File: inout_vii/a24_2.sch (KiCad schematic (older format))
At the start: 21 parts, among them U24010 74HC27, U24011 74LVC07, U24012 74HC02, U24013 74HC27, U24014 74HC02, U24015 74HC4002, U24016 74HC27, U24017 74LVC07, U24018 74HC02, U24019 74HC27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

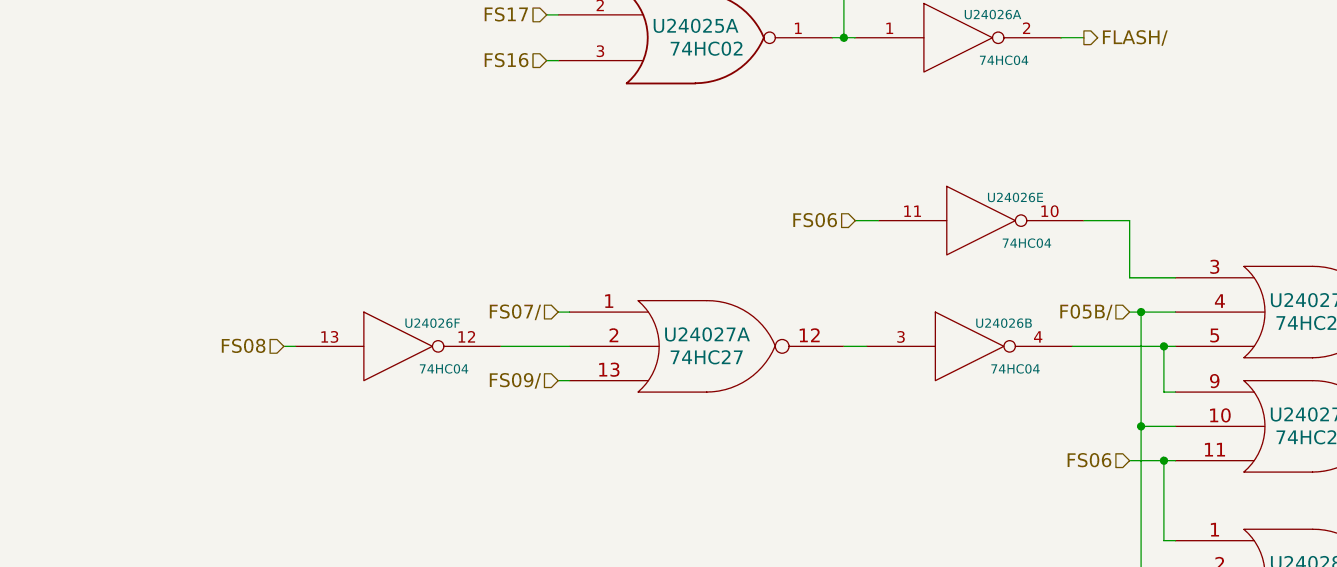
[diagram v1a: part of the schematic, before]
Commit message: Added some missing net names.
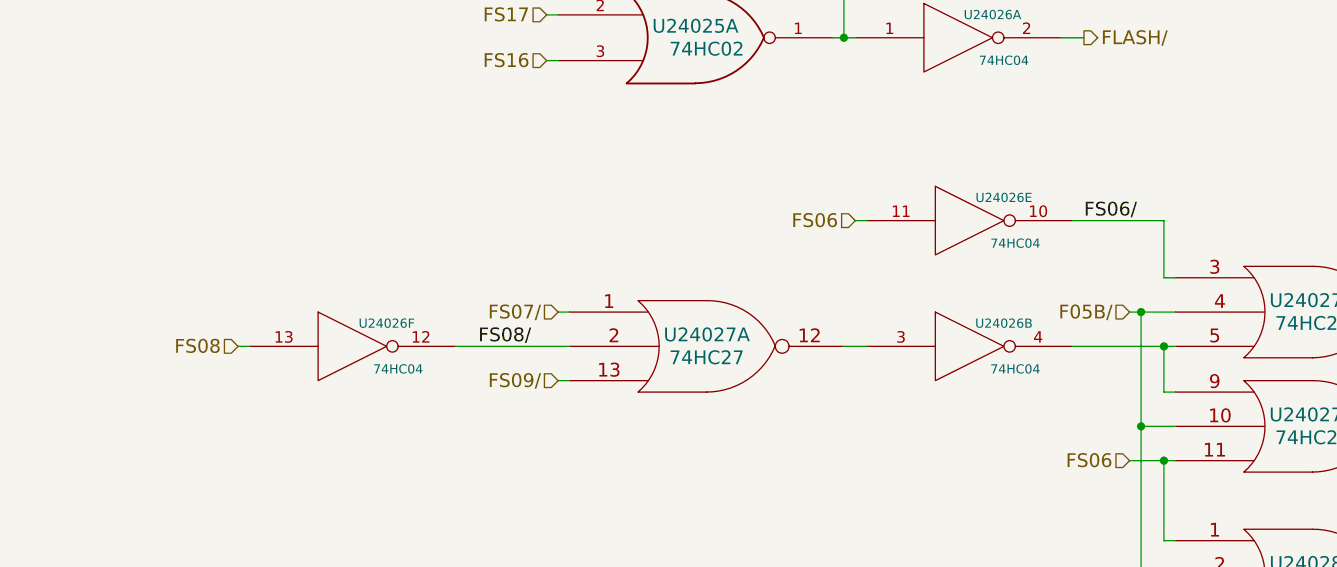
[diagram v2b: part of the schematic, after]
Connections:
- net FS08/: now reaches U24026.12, U24027.2
- net FS06/: now reaches U24026.10, U24027.3
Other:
- moved on the sheet: U24026E, U24026F
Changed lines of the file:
@@
 Wire Wire Line
 	9300 4300 9350 4300
-Text HLabel 8100 4450 0    60   Input ~ 0
+Text HLabel 7900 4450 0    60   Input ~ 0
 FS08
 Wire Wire Line
-	9050 4450 9350 4450
+	8850 4450 9350 4450
 Text HLabel 9300 4600 0    60   Input ~ 0
 FS09/
@@
 FS06
 Wire Wire Line
-	11800 4150 12000 4150
+	11950 4150 12000 4150
 Text HLabel 11800 4300 0    60   Input ~ 0
 F05B/
@@
 L 74HC04 U24026
 U 5 1 57212A45
-P 11150 3900
-F 0 "U24026" H 11300 4000 40  0000 C CNN
-F 1 "74HC04" H 11350 3800 40  0000 C CNN
-F 2 "" H 11150 3900 60  0000 C CNN
-F 3 "" H 11150 3900 60  0000 C CNN
-	5    11150 3900
-	1    0    0    -1
-$EndComp
-Wire Wire Line
-	10600 3900 10700 3900
-Wire Wire Line
-	11800 4150 11800 3900
-Wire Wire Line
-	11800 3900 11600 3900
+P 11100 3900
+F 0 "U24026" H 11250 4000 40  0000 C CNN
+F 1 "74HC04" H 11300 3800 40  0000 C CNN
+F 2 "" H 11100 3900 60  0000 C CNN
+F 3 "" H 11100 3900 60  0000 C CNN
+	5    11100 3900
+	1    0    0    -1
+$EndComp
+Wire Wire Line
+	10600 3900 10650 3900
+Wire Wire Line
+	11950 4150 11950 3900
+Wire Wire Line
+	11950 3900 11550 3900
 $Comp
 L 74HC04 U24026
 U 6 1 5721963E
-P 8600 4450
-F 0 "U24026" H 8750 4550 40  0000 C CNN
-F 1 "74HC04" H 8800 4350 40  0000 C CNN
-F 2 "" H 8600 4450 60  0000 C CNN
-F 3 "" H 8600 4450 60  0000 C CNN
-	6    8600 4450
-	1    0    0    -1
-$EndComp
-Wire Wire Line
-	8100 4450 8150 4450
+P 8400 4450
+F 0 "U24026" H 8550 4550 40  0000 C CNN
+F 1 "74HC04" H 8600 4350 40  0000 C CNN
+F 2 "" H 8400 4450 60  0000 C CNN
+F 3 "" H 8400 4450 60  0000 C CNN
+	6    8400 4450
+	1    0    0    -1
+$EndComp
+Wire Wire Line
+	7900 4450 7950 4450
+Text Label 8950 4450 0    60   ~ 0
+FS08/
+Text Label 11600 3900 0    60   ~ 0
+FS06/
 $EndSCHEMATC

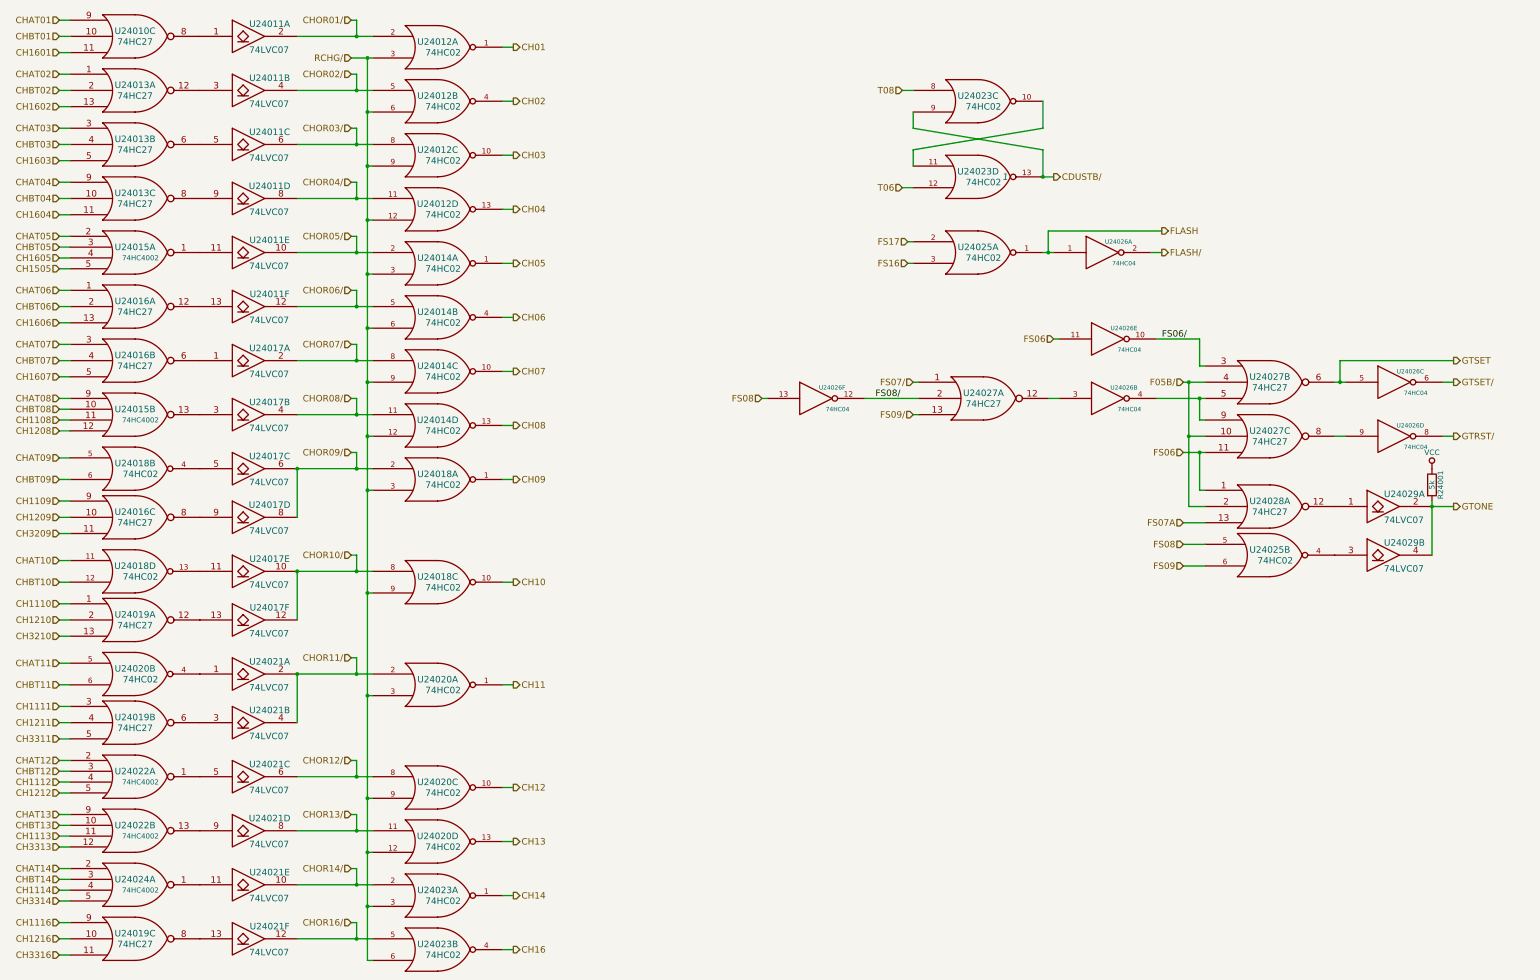
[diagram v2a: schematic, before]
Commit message: Fixed not->1-input nor in the rest of the modules.
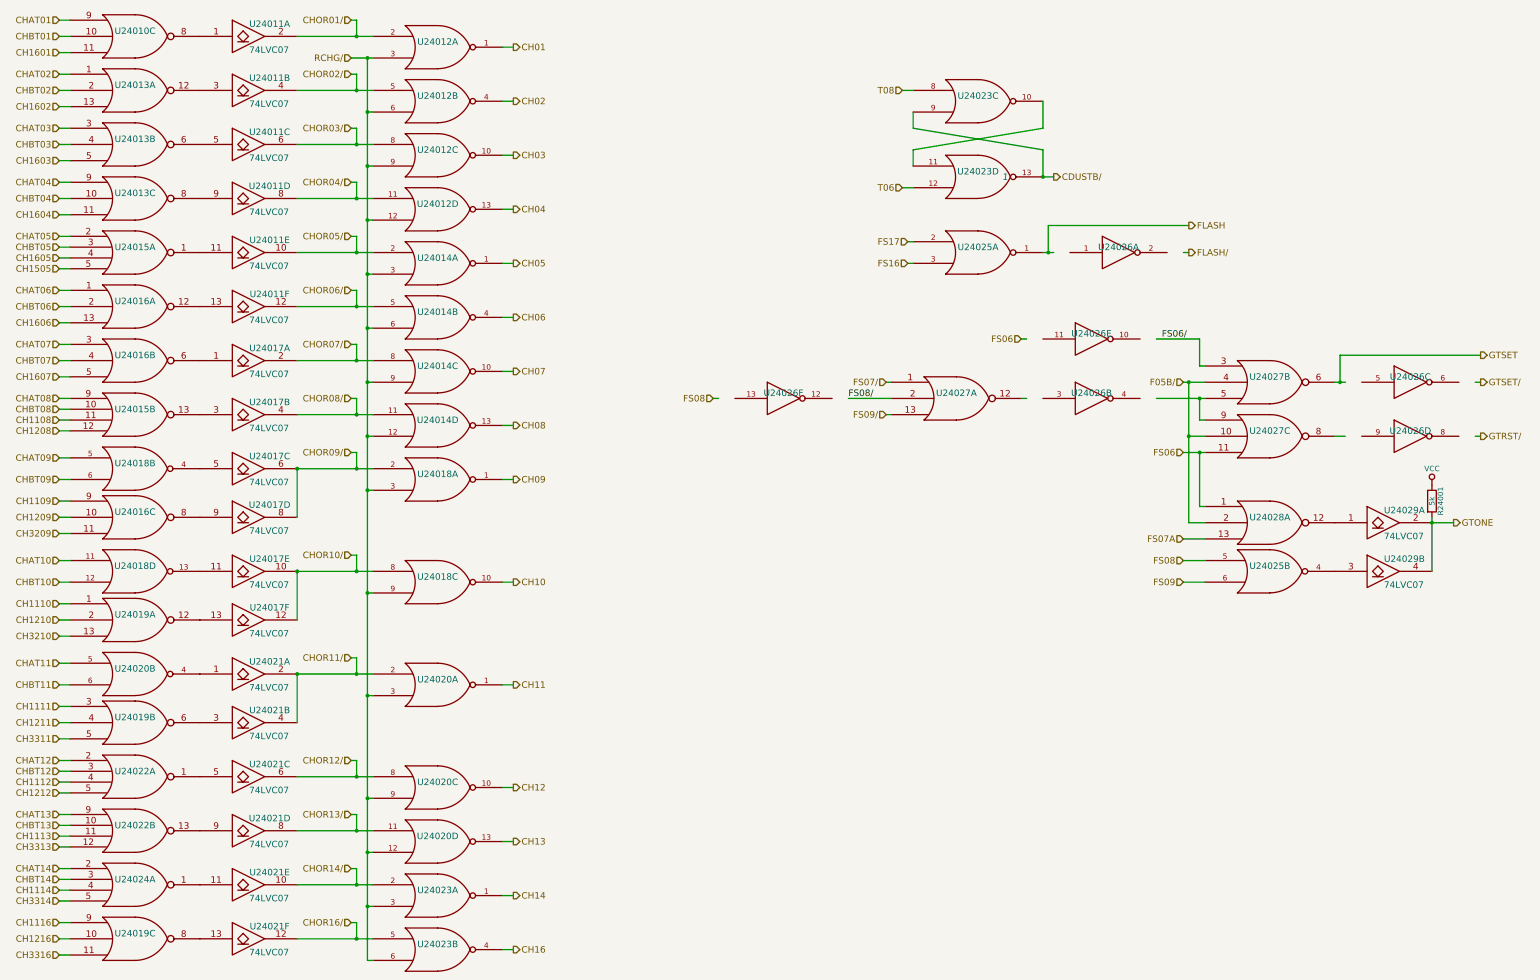
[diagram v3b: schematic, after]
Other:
- moved on the sheet: R24001, U24025B, U24026A, U24026B, U24026C, U24026D, U24026E, U24026F, U24027A, U24028A, U24029A, U24029B

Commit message: Updated power nets for Inout VII. Almost there...
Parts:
- renumbered U24010 to U24037
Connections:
- net labels added: +4VSW
- net labels removed: VCC
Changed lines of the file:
@@
 LIBS:contrib
 LIBS:valves
+LIBS:inout_vii-cache
 EELAYER 25 0
 EELAYER END
@@
 $EndDescr
 $Comp
-L 74HC27 U24010
-U 3 1 57171922
+L 74HC27 U24037
+U 1 1 57171922
 P 2100 1100
-F 0 "U24010" H 2100 1150 60  0000 C CNN
+F 0 "U24037" H 2100 1150 60  0000 C CNN
 F 1 "74HC27" H 2100 1050 60  0001 C CNN
 F 2 "" H 2100 1100 60  0000 C CNN
 F 3 "" H 2100 1100 60  0000 C CNN
-	3    2100 1100
+	1    2100 1100
 	1    0    0    -1
 $EndComp
@@
 	1    0    0    -1
 $EndComp
-$Comp
-L VCC #PWR03
-U 1 1 571BDF78
-P 14100 5250
-F 0 "#PWR03" H 14100 5100 50  0001 C CNN
-F 1 "VCC" H 14100 5400 50  0000 C CNN
-F 2 "" H 14100 5250 60  0000 C CNN
-F 3 "" H 14100 5250 60  0000 C CNN
-	1    14100 5250
-	1    0    0    -1
-$EndComp
 Wire Wire Line
 	14100 5600 14300 5600
@@
 Text Label 11600 3900 0    60   ~ 0
 FS06/
+$Comp
+L +4VSW #PWR04
+U 1 1 582BF2D4
+P 14100 5250
+F 0 "#PWR04" H 14100 5100 50  0001 C CNN
+F 1 "+4VSW" H 14100 5390 50  0000 C CNN
+F 2 "" H 14100 5250 60  0000 C CNN
+F 3 "" H 14100 5250 60  0000 C CNN
+	1    14100 5250
+	1    0    0    -1
+$EndComp
 $EndSCHEMATC
